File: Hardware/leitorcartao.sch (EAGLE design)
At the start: 166 parts, among them IC1 TL084, IC2 TL084, Q1 DMN3404, Q2 MMBT4401, Q3 MMBT4403, Q4 MMBT4401, Q5 MMBT4401, Q6 MMBT4401, Q7 MMBT4401, U1 LP2985-33DBVR, U2 TLV1117-50CDCYR, U3 SAMD20E14A-AUT, U4 MFRC52202HN1, X1 ANTENA, X2 MIFARE

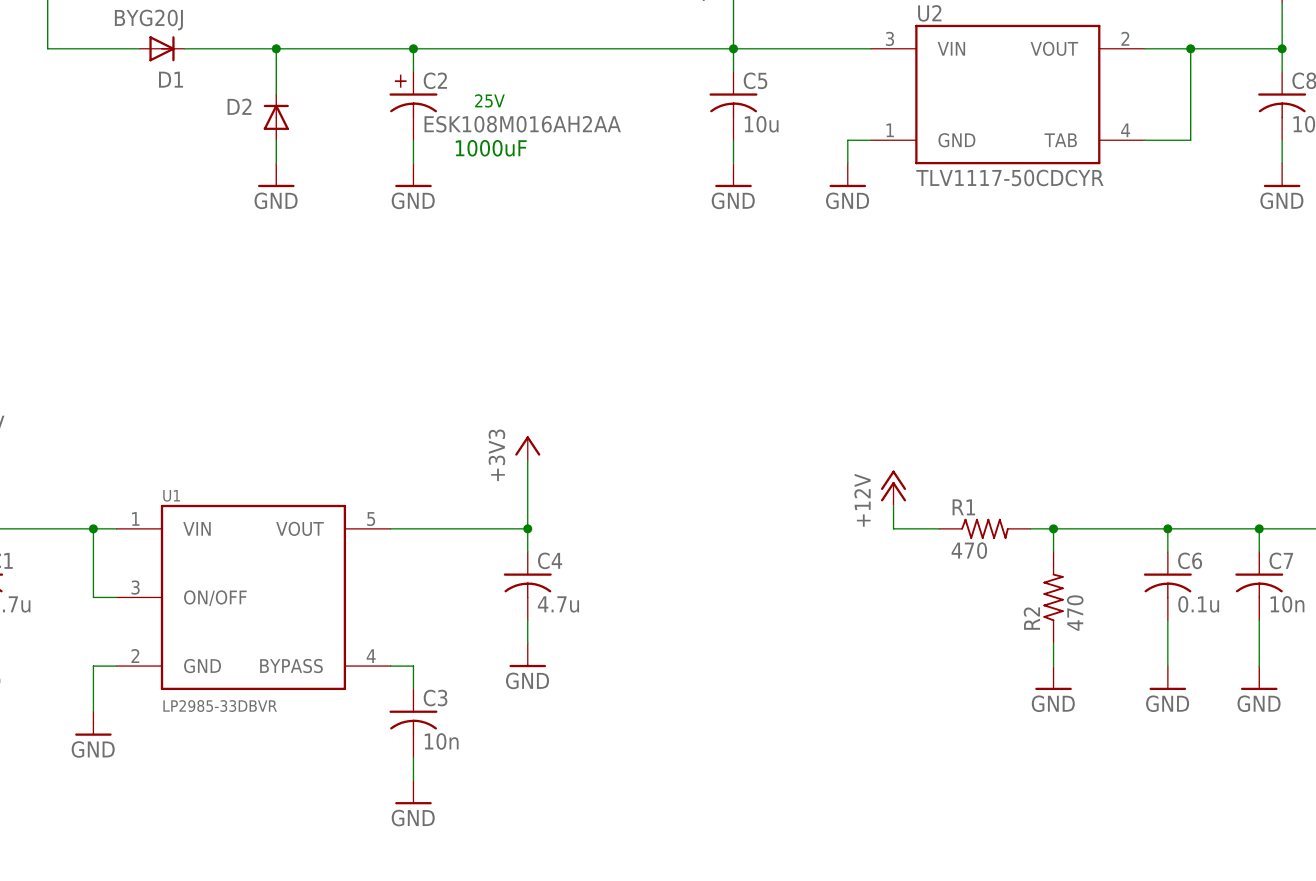
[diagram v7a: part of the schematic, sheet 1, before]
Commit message: Mudanças nos PN dos reguladores de tensão.
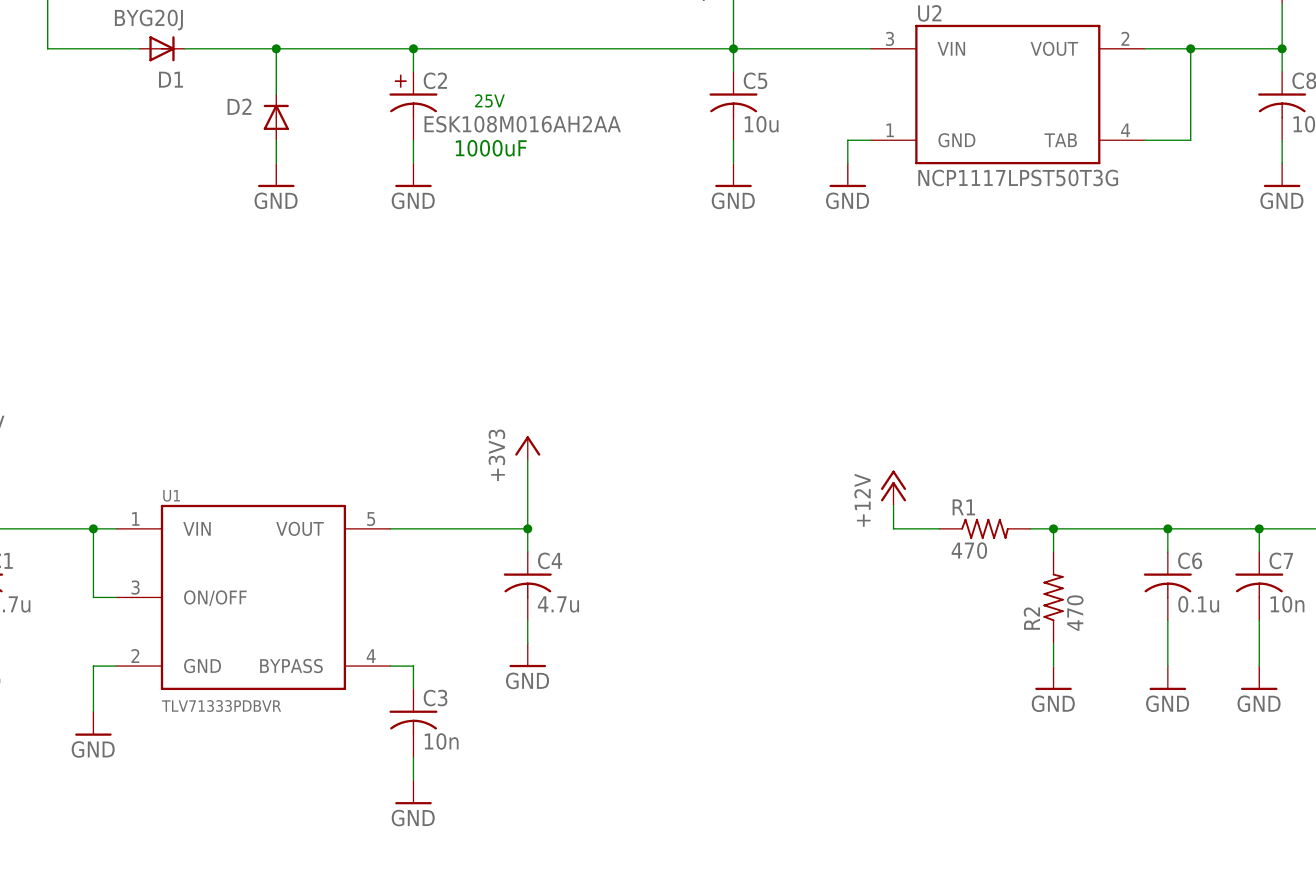
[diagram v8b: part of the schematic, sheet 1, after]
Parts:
- U1: value LP2985-33DBVR -> TLV71333PDBVR; ASK_PN LP2985-33DBVR -> TLV71333PDBVR; FSK_PN LP2985-33DBVR -> TLV71333PDBVR; MIFARE_PN LP2985-33DBVR -> TLV71333PDBVR; PSK_PN LP2985-33DBVR -> TLV71333PDBVR
- U2: value TLV1117-50CDCYR -> NCP1117LPST50T3G; ASK_PN TLV1117-50CDCYR -> NCP1117LPST50T3G; FSK_PN TLV1117-50CDCYR -> NCP1117LPST50T3G; MIFARE_PN TLV1117-50CDCYR -> NCP1117LPST50T3G; PSK_PN TLV1117-50CDCYR -> NCP1117LPST50T3G
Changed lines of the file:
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@@
 </part>
 <part name="+3V5" library="supply1" deviceset="+3V3" device=""/>
-<part name="U2" library="RFiD" deviceset="TLV1117-50CDCYR" device="">
+<part name="U2" library="RFiD" deviceset="TLV1117-50CDCYR" device="" value="NCP1117LPST50T3G">
 <attribute name="ASK" value="X"/>
 <attribute name="ASK_CUSTOMERPN" value="IC/5VREG"/>
-<attribute name="ASK_PN" value="TLV1117-50CDCYR"/>
+<attribute name="ASK_PN" value="NCP1117LPST50T3G"/>
 <attribute name="CUSTOMERPN" value=""/>
 <attribute name="FSK" value="X"/>
 <attribute name="FSK_CUSTOMERPN" value="IC/5VREG"/>
-<attribute name="FSK_PN" value="TLV1117-50CDCYR"/>
+<attribute name="FSK_PN" value="NCP1117LPST50T3G"/>
 <attribute name="MIFARE" value="X"/>
 <attribute name="MIFARE_CUSTOMERPN" value="IC/5VREG"/>
-<attribute name="MIFARE_PN" value="TLV1117-50CDCYR"/>
+<attribute name="MIFARE_PN" value="NCP1117LPST50T3G"/>
 <attribute name="PASSIVO" value=""/>
 <attribute name="PN1" value=""/>
 <attribute name="PSK" value="X"/>
 <attribute name="PSK_CUSTOMERPN" value="IC/5VREG"/>
-<attribute name="PSK_PN" value="TLV1117-50CDCYR"/>
+<attribute name="PSK_PN" value="NCP1117LPST50T3G"/>
 <attribute name="SPECIAL" value=""/>
 </part>
@@
 </part>
 <part name="SUPPLY12" library="supply2" deviceset="+5V" device=""/>
-<part name="U1" library="RFiD" deviceset="LP2985-33DBVR" device="">
+<part name="U1" library="RFiD" deviceset="LP2985-33DBVR" device="" value="TLV71333PDBVR">
 <attribute name="ASK" value="X"/>
 <attribute name="ASK_CUSTOMERPN" value="IC/3V3REG"/>
-<attribute name="ASK_PN" value="LP2985-33DBVR"/>
+<attribute name="ASK_PN" value="TLV71333PDBVR"/>
 <attribute name="CUSTOMERPN" value=""/>
 <attribute name="FSK" value="X"/>
 <attribute name="FSK_CUSTOMERPN" value="IC/3V3REG"/>
-<attribute name="FSK_PN" value="LP2985-33DBVR"/>
+<attribute name="FSK_PN" value="TLV71333PDBVR"/>
 <attribute name="MIFARE" value="X"/>
 <attribute name="MIFARE_CUSTOMERPN" value="IC/3V3REG"/>
-<attribute name="MIFARE_PN" value="LP2985-33DBVR"/>
+<attribute name="MIFARE_PN" value="TLV71333PDBVR"/>
 <attribute name="PASSIVO" value=""/>
 <attribute name="PN1" value=""/>
 <attribute name="PSK" value="X"/>
 <attribute name="PSK_CUSTOMERPN" value="IC/3V3REG"/>
-<attribute name="PSK_PN" value="LP2985-33DBVR"/>
-<attribute name="SPECIAL" value=""/>
-</part>
+<attribute name="PSK_PN" value="TLV71333PDBVR"/>
+<attribute name="SPECIAL" value=""/>
+</part>
